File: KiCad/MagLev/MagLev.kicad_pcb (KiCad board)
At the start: 2 copper layers, 120 x 120 mm, 204 parts, among them J1 FC681465S, J2 Programming header, J4 USB_B_Micro, Q1 ZX5T851GTA, Q10 ZX5T851GTA, Q11 MMBT3904, Q12 AOD442G, Q13 AOD442G, Q14 ZX5T851GTA, Q16 TEMT7000X01, Q18 ZX5T1951GTA, Q2 ZX5T1951GTA, Q3 ZX5T851GTA, Q4 ZX5T1951GTA, Q5 ZX5T1951GTA, Q6 ZX5T851GTA, Q7 ZX5T1951GTA, Q8 ZX5T851GTA, Q9 ZX5T1951GTA, U1 LM324, U10 X, U11 Y, U12 Z, U13 MCP1402, U14 MCP1402, U2 LM324, U3 L78L05_SO8, U4 TL431A, U5 LM393, U6 ATmega328P-A, U8 FT232RL, U9 LM1117MP-5.0, X1 L_Ferrite, X2 L_Ferrite, Y1 L_Ferrite, Y2 L_Ferrite, Y3 J49SMH-16MHz, Y5 L_Ferrite, Y6 L_Ferrite, Y8 L_Ferrite, Y9 L_Ferrite

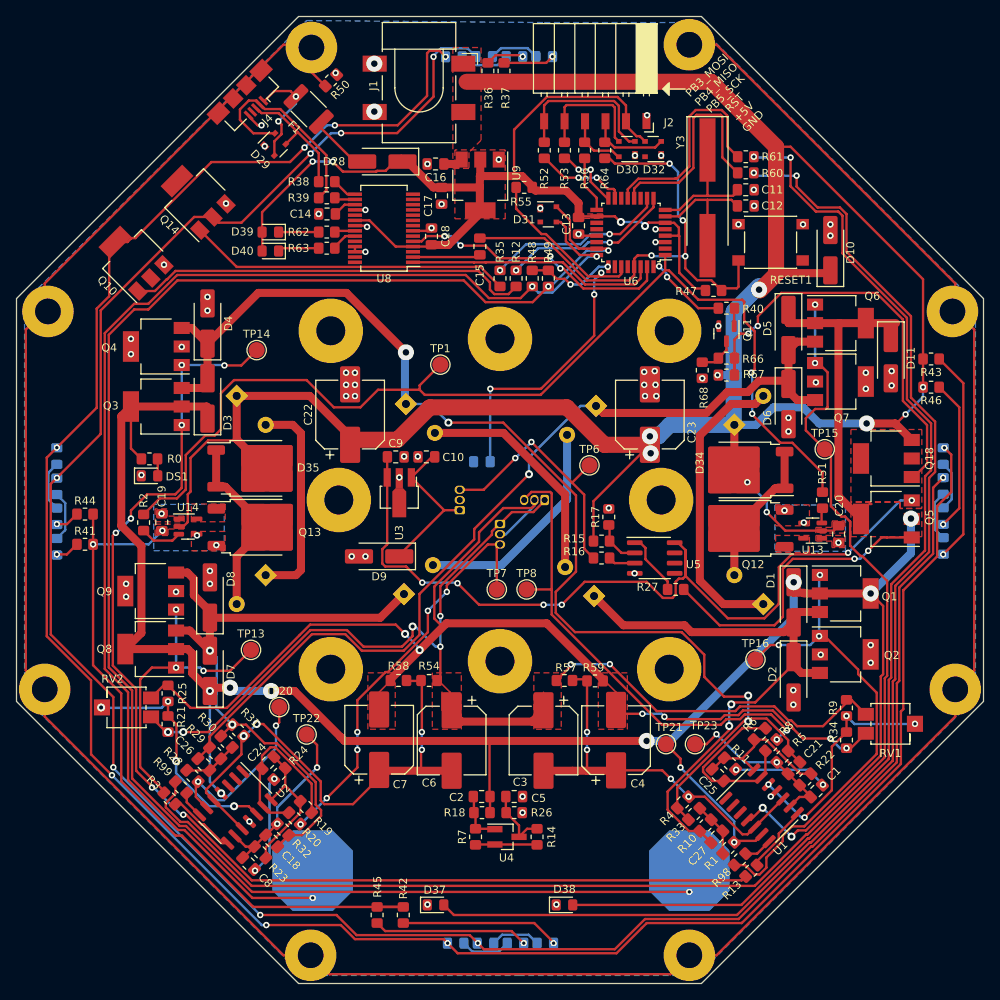
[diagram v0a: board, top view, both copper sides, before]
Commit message: Add decoupling caps to PWM switching Fets.
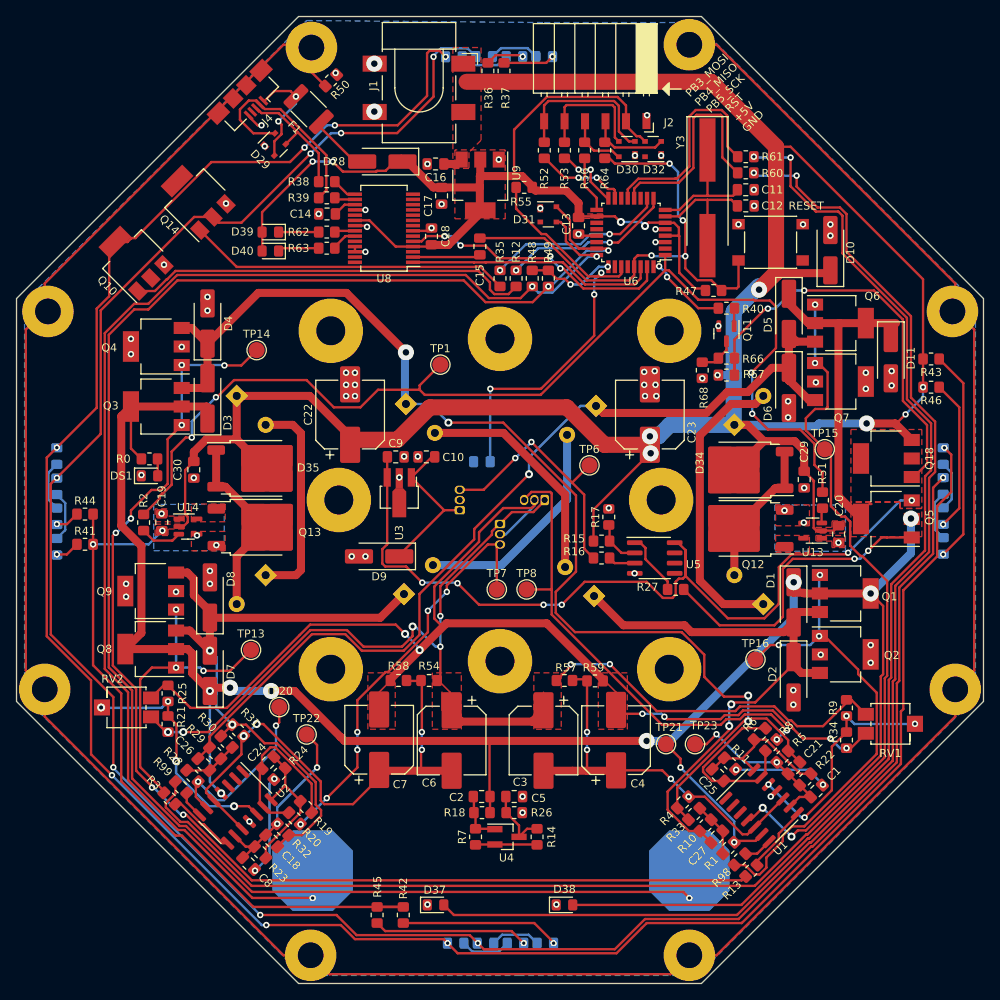
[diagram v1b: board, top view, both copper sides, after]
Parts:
- added C29: 4.7uF, Capacitor_SMD:C_0805_2012Metric_Pad1.18x1.45mm_HandSolder, F.Cu at (190.2, 99.1)
- added C30: 4.7uF, Capacitor_SMD:C_0805_2012Metric_Pad1.18x1.45mm_HandSolder, F.Cu at (114.4, 97.8)
- moved D5 2.00 mm to (188.3, 78.5)
- moved D6 2.00 mm to (188.3, 87.7)
- renumbered RESET1 to RESET
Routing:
- net VCC: track 380.6 -> 387.9 mm, vias 11 -> 9
- net /CoilPWM: track 132.1 -> 136.3 mm, vias 2 -> 4
- net /Y2: track 113.6 -> 115.2 mm
- net Net-(Q3-B): track 148.8 -> 147.5 mm
- net GND: vias 84 -> 86

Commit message: Review all footprints.
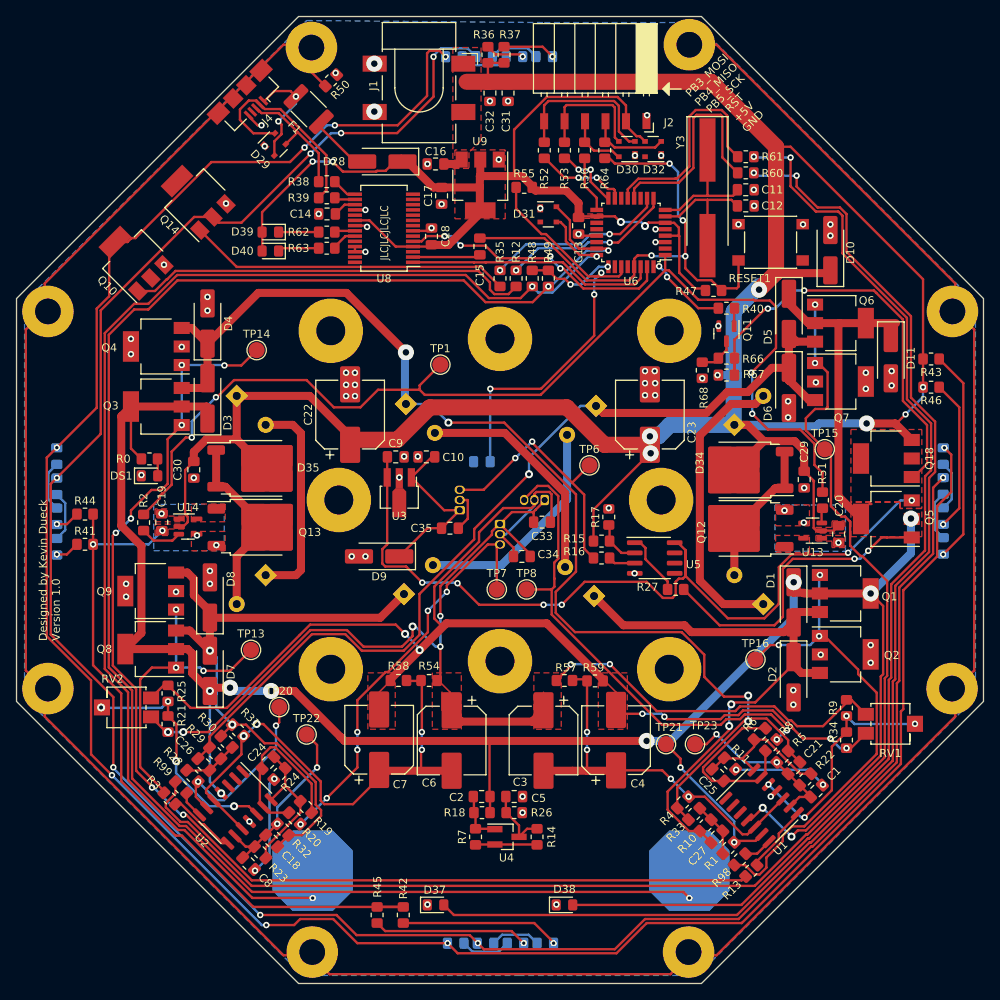
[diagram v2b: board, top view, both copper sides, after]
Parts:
- added C31: 4.7uF, Capacitor_SMD:C_0805_2012Metric_Pad1.18x1.45mm_HandSolder, F.Cu at (153.4, 51.1)
- added C32: 0.1uF, Capacitor_SMD:C_0805_2012Metric_Pad1.18x1.45mm_HandSolder, F.Cu at (151.2, 51.1)
- added C33: 0.1uF, Capacitor_SMD:C_0805_2012Metric_Pad1.18x1.45mm_HandSolder, F.Cu at (157.6, 104.3)
- added C34: 0.1uF, Capacitor_SMD:C_0805_2012Metric_Pad1.18x1.45mm_HandSolder, F.Cu at (155.1, 108.6)
- added C35: 0.1uF, Capacitor_SMD:C_0805_2012Metric_Pad1.18x1.45mm_HandSolder, F.Cu at (146.2, 105.1)
- D34, D35: value D -> MBRD1060
- U10: value X -> DRV5505
- U11: value Y -> DRV5505
- U12: value Z -> DRV5505
- moved R36 2.00 mm to (150.9, 46.4)
- moved R37 2.00 mm to (152.9, 46.4)
- moved H8 0.45 mm to (129.1, 157.7)
- moved H6 0.41 mm to (208.5, 125.0)
- moved H7 0.41 mm to (175.8, 157.7)
- moved H4 0.41 mm to (96.3, 125.0)
- turned Q16 to 0 degrees
- renumbered RESET to RESET1
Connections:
- Q16 pad 1: /MCU/LightSense -> GND
- Q16 pad 2: GND -> /MCU/LightSense
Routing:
- net /Vref-: track 148.4 -> 158.3 mm
- net /Vref+: track 143.0 -> 149.8 mm
- net GND: track 19.4 -> 24.3 mm, vias 86 -> 88
- net VCC: track 387.9 -> 392.3 mm
- net /Vreg: track 19.7 -> 21.5 mm
- net /H1: track 60.1 -> 61.7 mm
- net Net-(D13-K): track 286.3 -> 286.9 mm
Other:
- board text added: "Designed by Kevin Dueck Version 1.0"
- board text added: "JLCJLCJLCJLC"

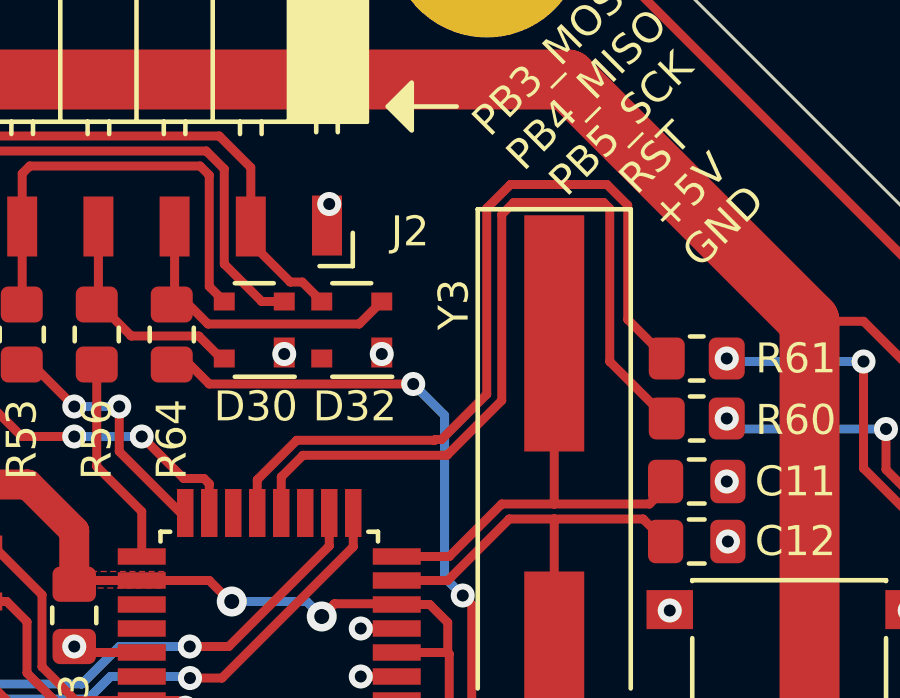
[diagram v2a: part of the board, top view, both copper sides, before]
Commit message: Set LED bias resistors. Move MCU status LEDs to PWM pins.
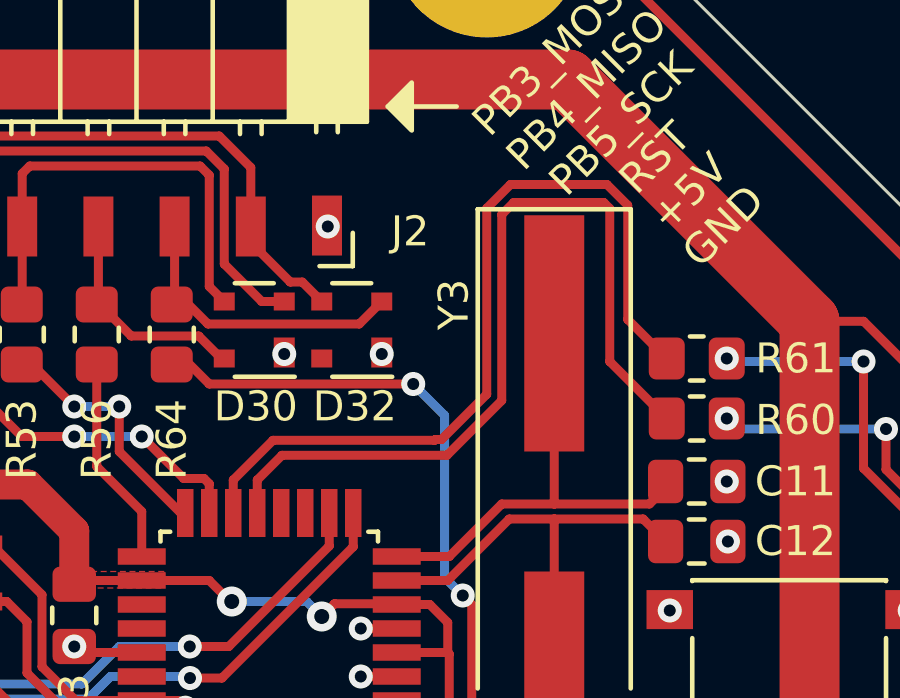
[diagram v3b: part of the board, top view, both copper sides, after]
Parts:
- C1, C8: value 105 -> 1uF
- C18, C21: value 4.5n -> 4.5nF
- C2, C5: value 104 -> .1uF
- C24, C25: value 0.4n -> 0.4nF
- C26, C27: value 30n -> 30nF
- D37, D38: value Blue -> Yellow
- R0: value 1k -> 1000
- R36, R37, R41, R42, R43, R44, R45, R46: value 1k -> 270
- R60, R61: value 1k -> 145
- R62, R63: value 1k -> 300
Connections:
- U6 pad 12: /MCU/LED1 -> unconnected-(U6-PB0-Pad12)
- U6 pad 13: /MCU/LED2 -> /MCU/LED1
- U6 pad 14: unconnected-(U6-PB2-Pad14) -> /MCU/LED2
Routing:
- net /MCU/LED2: track 27.1 -> 27.9 mm
- net /MCU/LED1: track 27.4 -> 28.2 mm
